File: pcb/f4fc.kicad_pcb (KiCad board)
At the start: 4 copper layers, 36 x 36 mm, 52 parts, among them P1 3V3, P3 USB_OTG, P4 CONN_02X04, P5 CONN_02X10, P6 RESET, P7 BOOT0, P9 5V, Q3 Q_NMOS_GSD, Q4 Q_NMOS_GSD, SW1 SW_PUSH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

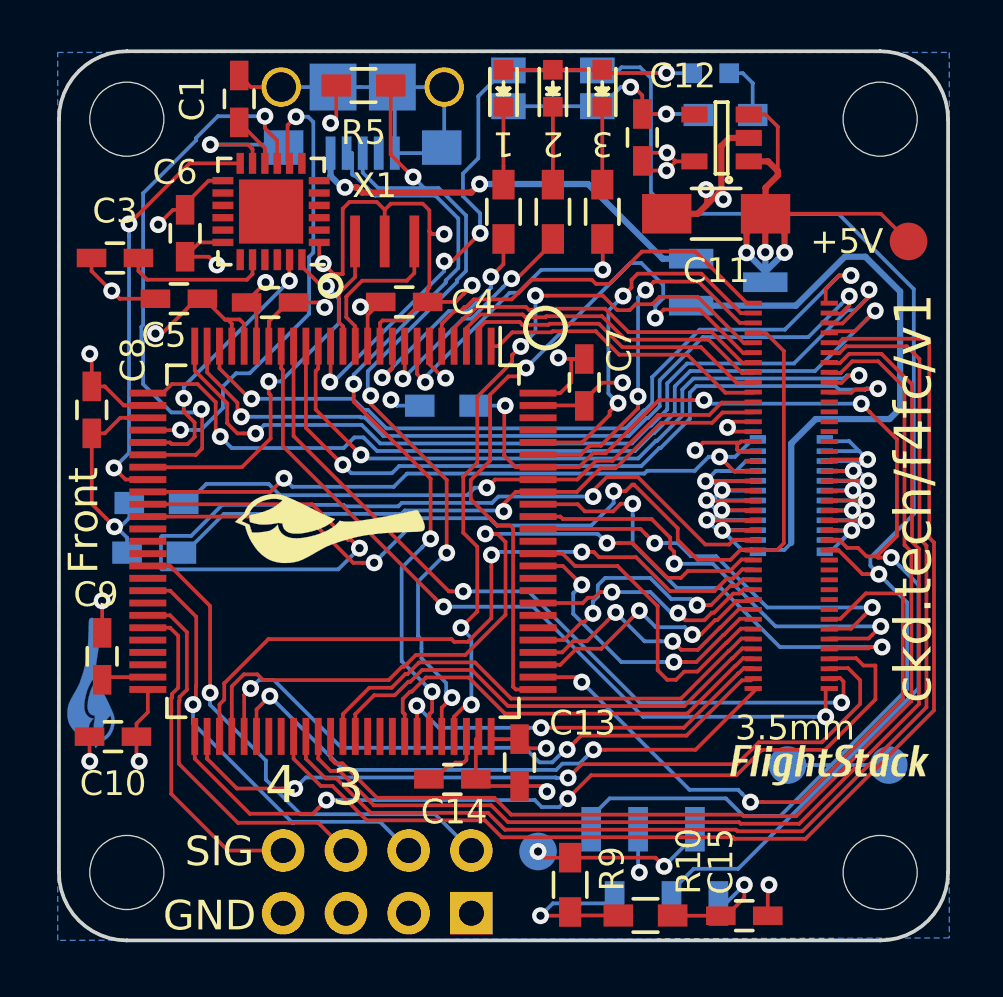
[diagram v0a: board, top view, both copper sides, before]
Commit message: F4FC v2 featuring corrected reset circuit.
Other changes:
* Route USB as differential pair.
* Add fiducials
* Remove copper pour from power connector
* New reset circuit
* Match up led nubmering to references
* Support current sensor through power connector
* remove 1.5k pull up from USB
* Pull down Boot1
* Add OSHW logo
* Move 3.5mm label out form under the FlightStack connector.
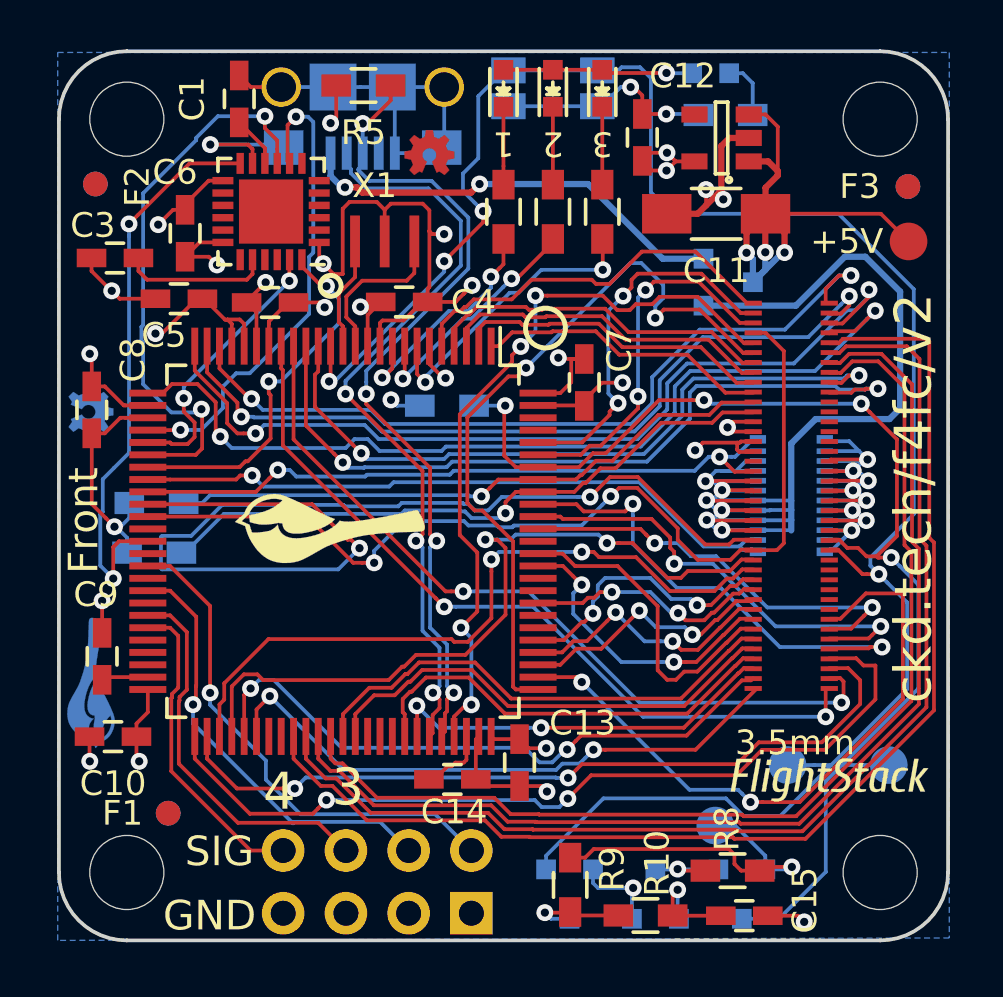
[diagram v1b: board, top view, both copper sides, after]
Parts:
- removed the G*** at (161.2, 118.9)
- added F1: 1mm, macrofab:Fiducial, F.Cu at (134.4, 120.8)
- added F2: 1mm, macrofab:Fiducial, F.Cu at (131.5, 95.4)
- added F3: 1mm, macrofab:Fiducial, F.Cu at (164.4, 95.5)
- added F4: 1mm, macrofab:Fiducial, B.Cu at (134.4, 120.8)
- added F5: 1mm, macrofab:Fiducial, B.Cu at (131.5, 95.4)
- added F6: 1mm, macrofab:Fiducial, B.Cu at (164.4, 95.5)
- added G***: LOGO, flightstack:flightstack_thin-8mm, F.Cu at (161.2, 119.5)
- added G***: OSHW, oshw:oshw-2mm, F.Cu at (145.0, 94.1)
- added G***: OSHW, oshw:oshw-2mm, B.Cu at (131.3, 104.6)
- added Q1: Q_PMOS_GSD, TO_SOT_Packages_SMD:SOT-23, B.Cu at (157.7, 124.1)
- added R8: 10k, Resistors_SMD:R_0603_HandSoldering, F.Cu at (157.3, 123.2)
- D1: renamed from D3; value LED -> Green
- D2: value LED -> Yellow
- D3: renamed from D1; value LED -> Red
- D4, Q3, Q4: footprint TO_SOT_Packages_SMD:SOT-23_Handsoldering -> TO_SOT_Packages_SMD:SOT-23
- D5: value PWR -> Red
- P5: footprint hirose-df40:DF40-20pin-Header -> DF40-20pin-Header
- moved P1 7.25 mm to (156.6, 121.3)
- moved Q3 2.14 mm to (150.7, 124.1)
- moved Q4 1.96 mm to (154.2, 124.1)
- renumbered R3 to R1, R1 to R3
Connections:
- net /USB_DM renamed /USB_D-
- net /USB_DP renamed /USB_D+
- P5 pad 1: +5V -> /Power/CURRENT
- Q4 pad 2: /Reset/BOOT0 -> GNDPWR
- Q4 pad 3: VDD -> Net-(Q1-Pad1)
- U2 pad 33: /MPU_INT -> /Power/CURRENT
- U2 pad 38: Net-(U2-Pad38) -> /MPU_INT
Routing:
- net /Power/CURRENT: track 0.00 -> 27.0 mm, vias 0 -> 1
- net VDD: track 70.5 -> 76.8 mm, vias 16 -> 15
- net /MPU_INT: track 17.2 -> 23.3 mm
- net Net-(Q1-Pad1): track 0.00 -> 3.71 mm, vias 0 -> 1
- net /Reset/RESET: track 78.7 -> 81.1 mm
- net Net-(Q3-Pad3): track 6.48 -> 4.36 mm
- net GNDPWR: track 131.0 -> 133.0 mm
- net /USB_D+: track 35.7 -> 33.9 mm
- net /Reset/BOOT0: track 51.1 -> 49.9 mm
- net Net-(C15-Pad1): track 5.24 -> 4.50 mm
- net /USB_D-: track 31.8 -> 31.1 mm
- net /TIM1_CH4: track 13.4 -> 12.8 mm
- net +5VA: track 17.2 -> 17.7 mm
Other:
- net class Default: clearance 0.1524 -> 0.14986
- rule trace_clearance: 0.1524 -> 0.14986
- board text added: "ckd.tech/f4fc/v2"
- board text removed: "ckd.tech/f4fc/v1"

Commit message: More changes to F4. Can't remember what.
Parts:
- removed the G*** at (145.0, 94.1)
- added G***: OSHW, oshw:oshw-4mm, F.Cu at (142.3, 92.3)
- added P2: CONN_01X01, Measurement_Points:Measurement_Point_Square-SMD-Pad_Small, B.Cu at (164.5, 97.5)
- R5: value 1.5k -> 10k
- X1: value CRYSTAL_SMD -> 8mhz
- moved R5 21.0 mm to (131.1, 109.2), turned to 270 degrees
- moved C8 0.69 mm to (131.1, 103.9)
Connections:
- PORT_OUT1 pad 1: /TIM9_CH2 -> /TIM8_CH3
- PORT_OUT1 pad 2: /TIM11_CH1 -> /TIM3_CH4
- PORT_OUT1 pad 25: /TIM3_CH3_UART7_TX -> Net-(PORT_OUT1-Pad25)
- PORT_OUT1 pad 26: /TIM3_CH3_UART7_RX -> Net-(PORT_OUT1-Pad26)
- PORT_OUT1 pad 3: /TIM10_CH1 -> /TIM2_CH4
- PORT_OUT1 pad 4: /TIM3_CH3_UART7_RX -> /TIM11_CH1
- R5 pad 1: /USB_D+ -> Net-(R5-Pad1)
- R5 pad 2: VDD -> GNDPWR
- U2 pad 1: /GPIO6 -> /GPIO5
- U2 pad 2: /GPIO5 -> /GPIO4
- U2 pad 3: /GPIO4 -> /GPIO3
- U2 pad 35: /TIM3_CH3_UART7_TX -> Net-(U2-Pad35)
- U2 pad 36: /TIM3_CH3_UART7_RX -> Net-(U2-Pad36)
- U2 pad 37: Net-(U2-Pad37) -> Net-(R5-Pad1)
- U2 pad 4: /GPIO3 -> Net-(U2-Pad4)
- U2 pad 48: Net-(U2-Pad48) -> /TIM2_CH4
- U2 pad 5: /TIM9_CH2 -> Net-(U2-Pad5)
- U2 pad 65: Net-(U2-Pad65) -> /TIM8_CH3
- U2 pad 66: Net-(U2-Pad66) -> /TIM3_CH4
- U2 pad 95: /TIM10_CH1 -> /GPIO6
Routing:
- net /TIM3_CH3_UART7_TX: track 45.5 -> 0.00 mm, vias 2 -> 0
- net /TIM2_CH4: track 0.00 -> 45.5 mm, vias 0 -> 2
- net /TIM3_CH3_UART7_RX: track 39.4 -> 0.00 mm, vias 2 -> 0
- net /TIM8_CH3: track 0.00 -> 31.3 mm, vias 0 -> 4
- net /TIM3_CH4: track 0.00 -> 31.0 mm, vias 0 -> 4
- net /TIM9_CH2: track 15.7 -> 0.00 mm
- net /TIM10_CH1: track 14.9 -> 0.00 mm, vias 2 -> 0
- net GNDPWR: track 133.0 -> 140.5 mm, vias 28 -> 29
- net /USB_D+: track 33.9 -> 30.6 mm, vias 4 -> 3
- net Net-(R5-Pad1): track 0.00 -> 3.08 mm
- net /LED0: track 12.1 -> 14.0 mm
- net /GPIO6: track 11.9 -> 10.1 mm
- net /GPIO2_13_SWDIO: track 30.3 -> 28.8 mm
- net VDD: track 76.8 -> 78.4 mm, vias 15 -> 14
- net /GPIO1_14_SWCLK: track 30.1 -> 28.6 mm
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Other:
- board text added: "ckd.tech/f4fc/v4"
- board text removed: "ckd.tech/f4fc/v2"

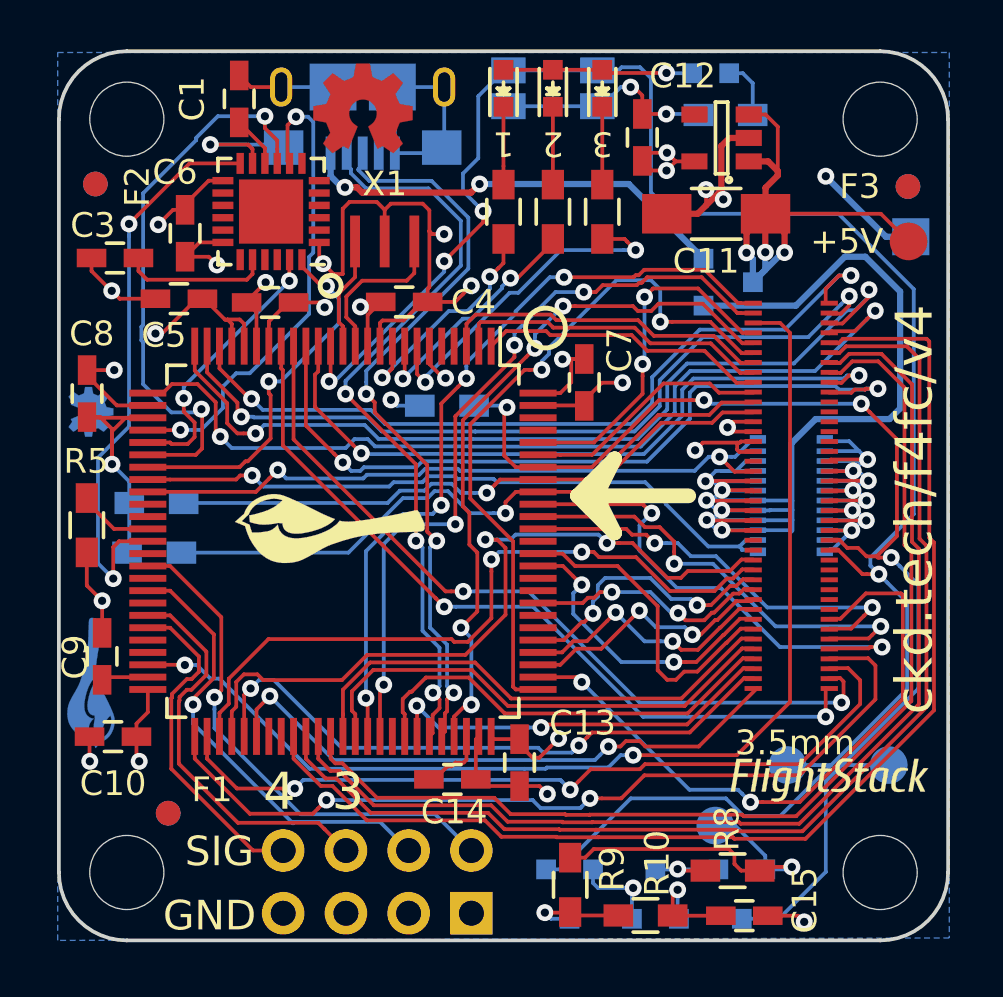
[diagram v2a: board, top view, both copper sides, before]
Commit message: Rebrand everything to Polystack and increment versions.
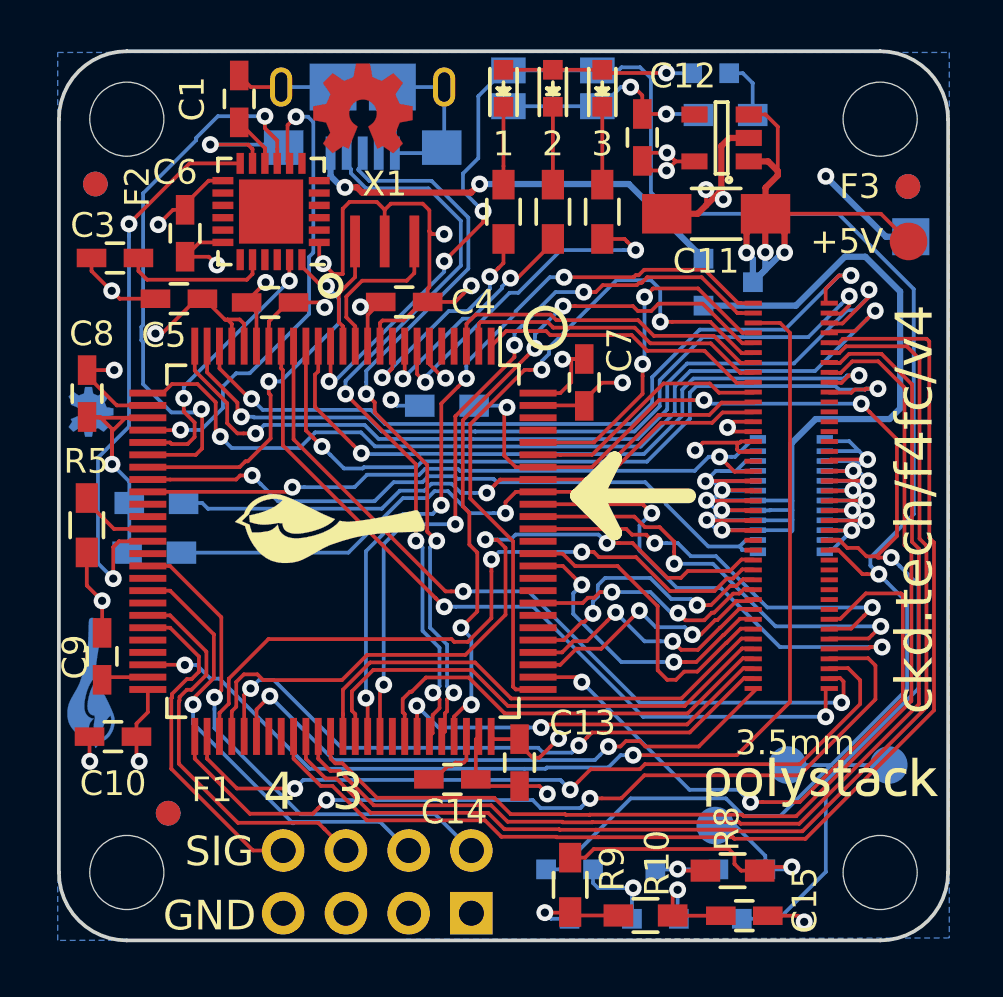
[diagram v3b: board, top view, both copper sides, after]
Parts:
- removed the G*** at (161.2, 119.5)
- added svg2mod: G***, polystack:polystack-medium-0.5, F.Cu at (160.9, 119.6)
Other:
- rule pad_to_mask_clearance: 0.2 -> 0.0762
- board text added: "GND Outside"
- board text added: "f4fc v4"
- board text removed: "Top GND"
- board text removed: "f4fc v1"

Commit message: Final gerbers for test manufacturing run.
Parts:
- P3: footprint fci:Mini-USB-B -> fci:Mini-USB-B-EDGE
- moved P3 1.20 mm to (142.3, 92.7)
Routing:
- net GNDPWR: track 140.5 -> 148.2 mm, vias 29 -> 31
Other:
- outline, holes or cut-outs redrawn

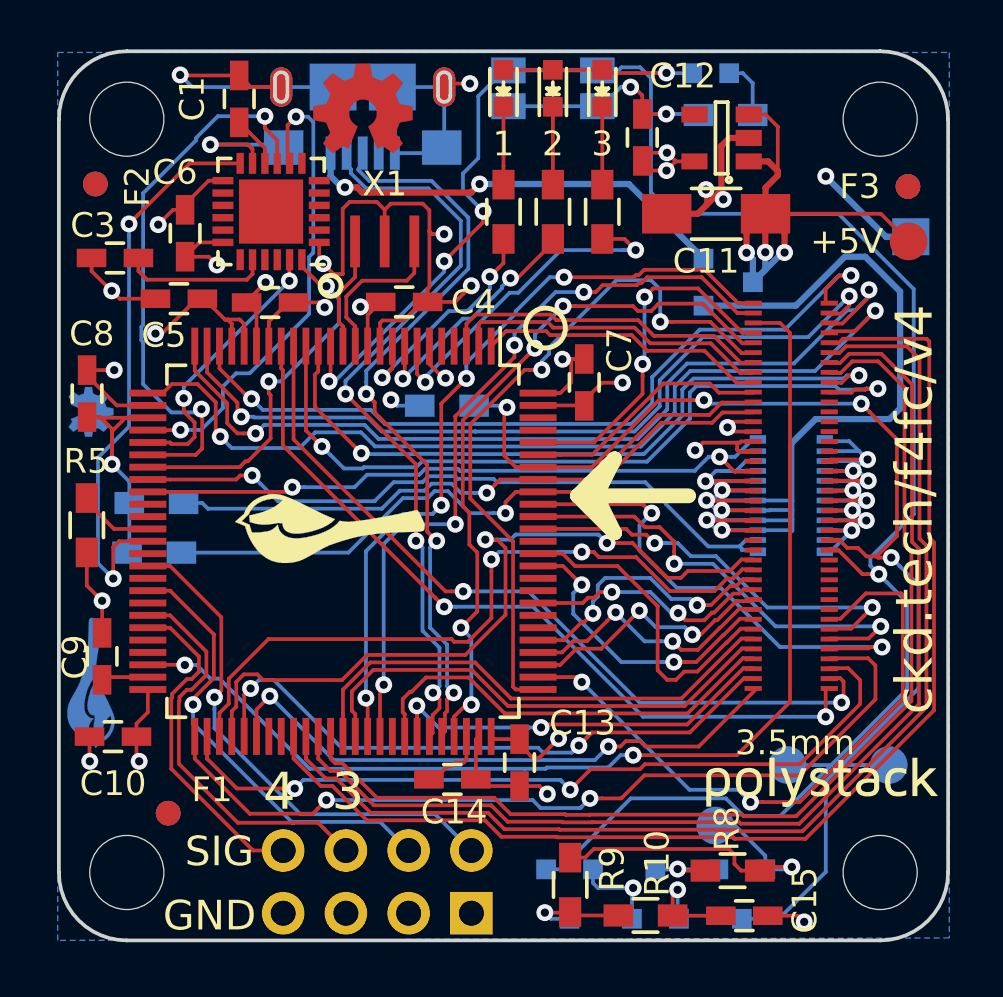
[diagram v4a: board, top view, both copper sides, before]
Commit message: Update polystack logo to bold variant and bump version number.
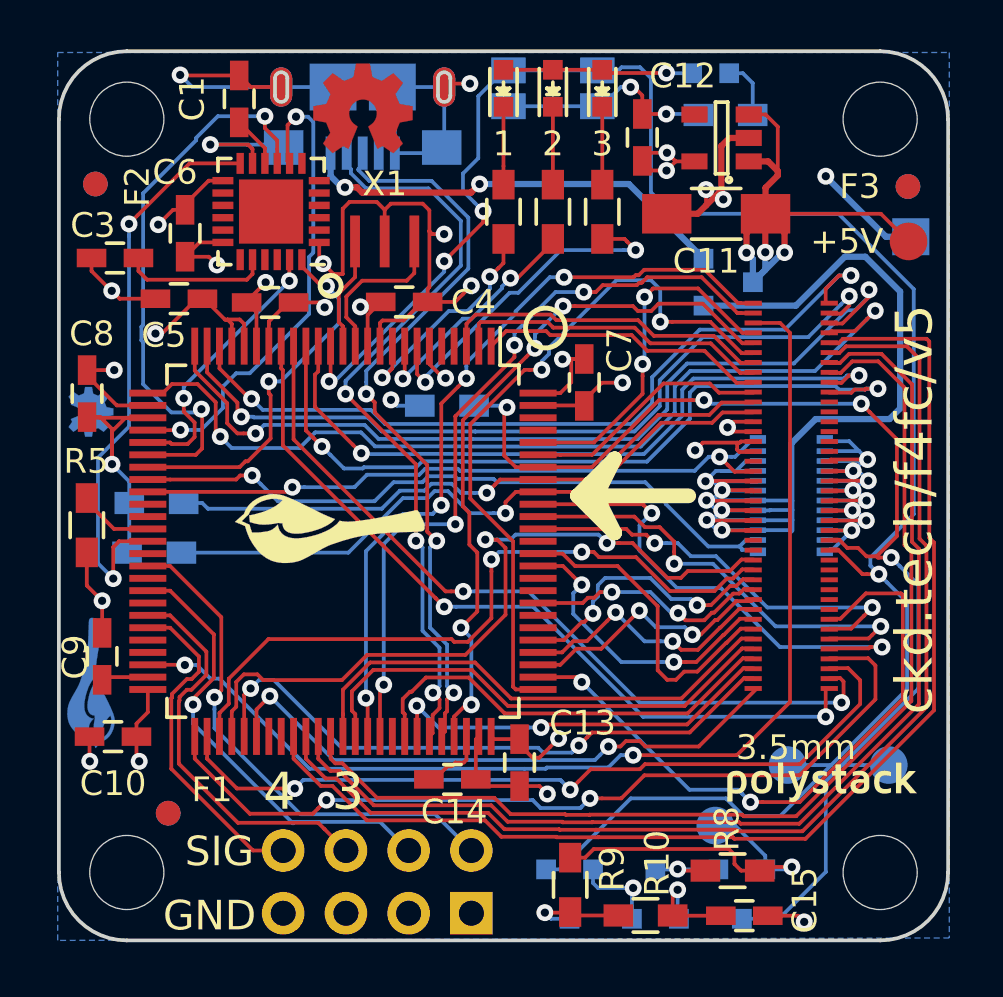
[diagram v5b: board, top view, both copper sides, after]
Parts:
- svg2mod: footprint polystack:polystack-medium-0.5 -> polystack:polystack-bold-0.4
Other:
- board text added: "ckd.tech/f4fc/v5"
- board text removed: "ckd.tech/f4fc/v4"

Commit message: Add license information to many files. PCB design files are CC-BY and code is MIT license.
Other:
- board text added: "Copyright 2016 Chickadee Tech LLC, <add attributions here> This work is licensed under the Creative Commons Attribution 4.0 International License. To view a copy of this license, visit http://creativecommons.org/licenses/by/4.0/ or send a letter to Creative Commons, PO Box 1866, Mountain View, CA 94042, USA."
- board text added: "Remove all Chickadee Tech LLC trademarks before making your own board. The Chickadee logo and Polystack logo are owned by Chickadee Tech LLC. You may license the Polystack logo for free by emailing support@chickadee.tech and receiving express written permission from Chickadee Tech LLC."
- board text added: "The gear logo is a mark designating open source hardware. Remove it if your design does not comply with the open source hardware definition."
- board text added: "f4fc"
- board text removed: "f4fc v4"
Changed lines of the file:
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@@
     (area 118.127143 74.1 214.642858 178)
     (thickness 1.6)
-    (drawings 70)
+    (drawings 77)
     (tracks 1664)
     (zones 0)
@@
     (40 Dwgs.User user)
     (41 Cmts.User user)
-    (42 Eco1.User user hide)
+    (42 Eco1.User user)
     (43 Eco2.User user)
     (44 Edge.Cuts user)
@@
       (xy 2.990233 0.444493)) (layer F.SilkS) (width 0))
   )
+  (gr_text "Copyright 2016 Chickadee Tech LLC, <add attributions here>\n\nThis work is licensed under the Creative Commons Attribution 4.0 International License.\nTo view a copy of this license, visit http://creativecommons.org/licenses/by/4.0/\nor send a letter to Creative Commons, PO Box 1866, Mountain View, CA 94042, USA." (at 178.61 173.54) (layer Cmts.User)
+    (effects (font (size 1.5 1.5) (thickness 0.3)) (justify left))
+  )
+  (gr_line (start 129.55 116.34) (end 109.59 109.04) (layer Cmts.User) (width 0.4))
+  (gr_line (start 109.53 109.04) (end 156.23 119.54) (layer Cmts.User) (width 0.4))
+  (gr_line (start 136.27 108.91) (end 109.53 109.04) (layer Cmts.User) (width 0.4))
+  (gr_line (start 140.4 91.93) (end 101.05 84.22) (layer Cmts.User) (width 0.4))
+  (gr_text "The gear logo is a mark designating open\nsource hardware. Remove it if your design\ndoes not comply with the open source\nhardware definition." (at 69.99 80.83) (layer Cmts.User)
+    (effects (font (size 1.5 1.5) (thickness 0.3)) (justify left))
+  )
+  (gr_text "Remove all Chickadee Tech LLC trademarks\nbefore making your own board. The\nChickadee logo and Polystack logo\nare owned by Chickadee Tech LLC.\n\nYou may license the Polystack logo for\nfree by emailing support@chickadee.tech\nand receiving express written permission\nfrom Chickadee Tech LLC." (at 68.86 110.42) (layer Cmts.User)
+    (effects (font (size 1.5 1.5) (thickness 0.3)) (justify left))
+  )
   (gr_circle (center 157.35 105) (end 157.55 105) (layer B.SilkS) (width 0.4))
   (gr_line (start 145.35 91.1) (end 145.35 91.8) (layer Edge.Cuts) (width 0.15))
@@
   (gr_line (start 166 92.75) (end 166 123.25) (angle 90) (layer Edge.Cuts) (width 0.15))
   (gr_line (start 132.75 90) (end 163.25 90) (angle 90) (layer Edge.Cuts) (width 0.15))
-  (gr_text "f4fc v4" (at 187.25 174.25) (layer Cmts.User)
-    (effects (font (size 5 5) (thickness 0.5)) (justify left))
+  (gr_text f4fc (at 187.86 190.07) (layer Cmts.User)
+    (effects (font (size 3 3) (thickness 0.5)) (justify left))
   )
   (segment (start 131.907101 109.592899) (end 132.25 109.25) (width 0.1524) (layer In2.Cu) (net 0))
